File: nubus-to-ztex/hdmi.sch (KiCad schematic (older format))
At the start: 10 parts, among them J5 10029449-111RLF (HDMI A), U9 TPD12S016PWR

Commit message: some BoM optimization
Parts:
- C20: MPN CC0603KRX7R8BB103 -> 0603B103K500NT; URL https://www.lcsc.com/product-detail/Multilayer-Ceramic-Capacitors-MLCC-SMD-SMT_YAGEO-CC0603KRX7R8BB103_C327204.html -> https://www.lcsc.com/product-detail/Multilayer-Ceramic-Capacitors-MLCC-SMD-SMT_FH-Guangdong-Fenghua-Advanced-Tech-0603B103K500NT_C57112.html
- C22, C23, C24: MPN CC0603KRX7R8BB104 -> CC0603KRX7R9BB104; URL https://www.lcsc.com/product-detail/Multilayer-Ceramic-Capacitors-MLCC-SMD-SMT_YAGEO-CC0603KRX7R8BB104_C92490.html -> https://www.lcsc.com/product-detail/Multilayer-Ceramic-Capacitors-MLCC-SMD-SMT_YAGEO-CC0603KRX7R9BB104_C14663.html
- C7: MPN C0805V103KCRACTU -> C0805X103K501T; MPN-ALT (none) -> C0805V103KCRACTU; MPN-ALT2 (none) -> TCC0805X7R103K501FT; URL https://www.lcsc.com/product-detail/Multilayer-Ceramic-Capacitors-MLCC-SMD-SMT_KEMET-C0805V103KCRACTU_C2170011.html -> https://www.lcsc.com/product-detail/Multilayer-Ceramic-Capacitors-MLCC-SMD-SMT_IHHEC-HOLY-STONE-ENTERPRISE-CO-LTD-C0805X103K501T_C105950.html; URL-ALT (none) -> https://www.lcsc.com/product-detail/Multilayer-Ceramic-Capa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; URL-ALT2 (none) -> https://www.lcsc.com/product-detail/Multilayer-Ceramic-Capa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
- R9: value 1M 500V 2512 -> 1M 500V 1206; footprint Resistor_SMD:R_2512_6332Metric -> Resistor_SMD:R_1206_3216Metric; MPN AS25J1004ET -> HR1206J1M00P05Z; MPN-ALT (none) -> KTR18EZPF1004; URL https://www.lcsc.com/product-detail/Chip-Resistor-Surface-Mount_Ohmite-AS25J1004ET_C2546765.html -> https://www.lcsc.com/product-detail/Chip-Resistor-Surface-Mount_Ever-Ohms-Tech-HR1206J1M00P05Z_C175518.html; URL-ALT (none) -> https://www.lcsc.com/product-detail/Chip-Resistor-Surface-M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
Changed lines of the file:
@@
 F 3 "" H 7300 1700 50  0000 C CNN
 F 4 "www.yageo.com" H 7300 1700 50  0001 C CNN "MNF1_URL"
-F 5 "CC0603KRX7R8BB104" H 7300 1700 50  0001 C CNN "MPN"
+F 5 "CC0603KRX7R9BB104" H 7300 1700 50  0001 C CNN "MPN"
 F 6 "603-CC603KRX7R8BB104" H 7300 1700 50  0001 C CNN "Mouser"
 F 7 "?" H 7300 1700 50  0001 C CNN "Digikey"
@@
 F 9 "?" H 7300 1700 50  0001 C CNN "Koncar"
 F 10 "TB" H 7300 1700 50  0001 C CNN "Side"
-F 11 "https://www.lcsc.com/product-detail/Multilayer-Ceramic-Capacitors-MLCC-SMD-SMT_YAGEO-CC0603KRX7R8BB104_C92490.html" H 3000 6050 50  0001 C CNN "URL"
+F 11 "https://www.lcsc.com/product-detail/Multilayer-Ceramic-Capacitors-MLCC-SMD-SMT_YAGEO-CC0603KRX7R9BB104_C14663.html" H 3000 6050 50  0001 C CNN "URL"
 	1    7300 1700
 	1    0    0    -1
@@
 F 3 "" H 2250 1600 50  0000 C CNN
 F 4 "www.yageo.com" H 2250 1600 50  0001 C CNN "MNF1_URL"
-F 5 "CC0603KRX7R8BB104" H 2250 1600 50  0001 C CNN "MPN"
+F 5 "CC0603KRX7R9BB104" H 2250 1600 50  0001 C CNN "MPN"
 F 6 "603-CC603KRX7R8BB104" H 2250 1600 50  0001 C CNN "Mouser"
 F 7 "?" H 2250 1600 50  0001 C CNN "Digikey"
@@
 F 9 "?" H 2250 1600 50  0001 C CNN "Koncar"
 F 10 "TB" H 2250 1600 50  0001 C CNN "Side"
-F 11 "https://www.lcsc.com/product-detail/Multilayer-Ceramic-Capacitors-MLCC-SMD-SMT_YAGEO-CC0603KRX7R8BB104_C92490.html" H 2250 1600 50  0001 C CNN "URL"
+F 11 "https://www.lcsc.com/product-detail/Multilayer-Ceramic-Capacitors-MLCC-SMD-SMT_YAGEO-CC0603KRX7R9BB104_C14663.html" H 2250 1600 50  0001 C CNN "URL"
 	1    2250 1600
 	0    1    1    0
@@
 F 3 "" H 2450 1900 50  0000 C CNN
 F 4 "www.yageo.com" H 2450 1900 50  0001 C CNN "MNF1_URL"
-F 5 "CC0603KRX7R8BB104" H 2450 1900 50  0001 C CNN "MPN"
+F 5 "CC0603KRX7R9BB104" H 2450 1900 50  0001 C CNN "MPN"
 F 6 "603-CC603KRX7R8BB104" H 2450 1900 50  0001 C CNN "Mouser"
 F 7 "?" H 2450 1900 50  0001 C CNN "Digikey"
@@
 F 9 "?" H 2450 1900 50  0001 C CNN "Koncar"
 F 10 "TB" H 2450 1900 50  0001 C CNN "Side"
-F 11 "https://www.lcsc.com/product-detail/Multilayer-Ceramic-Capacitors-MLCC-SMD-SMT_YAGEO-CC0603KRX7R8BB104_C92490.html" H 3000 6050 50  0001 C CNN "URL"
+F 11 "https://www.lcsc.com/product-detail/Multilayer-Ceramic-Capacitors-MLCC-SMD-SMT_YAGEO-CC0603KRX7R9BB104_C14663.html" H 3000 6050 50  0001 C CNN "URL"
 	1    2450 1900
 	0    1    1    0
@@
 F 3 "" H 2250 1100 50  0000 C CNN
 F 4 "www.yageo.com" H 2250 1100 50  0001 C CNN "MNF1_URL"
-F 5 "CC0603KRX7R8BB103" H 2250 1100 50  0001 C CNN "MPN"
+F 5 "0603B103K500NT" H 2250 1100 50  0001 C CNN "MPN"
 F 6 "603-CC603KRX7R8BB103" H 2250 1100 50  0001 C CNN "Mouser"
-F 7 "https://www.lcsc.com/product-detail/Multilayer-Ceramic-Capacitors-MLCC-SMD-SMT_YAGEO-CC0603KRX7R8BB103_C327204.html" H 2250 1100 50  0001 C CNN "URL"
+F 7 "https://www.lcsc.com/product-detail/Multilayer-Ceramic-Capacitors-MLCC-SMD-SMT_FH-Guangdong-Fenghua-Advanced-Tech-0603B103K500NT_C57112.html" H 2250 1100 50  0001 C CNN "URL"
 	1    2250 1100
 	0    1    1    0
@@
 F 2 "Capacitor_SMD:C_0805_2012Metric" H 8238 4500 50  0001 C CNN
 F 3 "~" H 8200 4650 50  0001 C CNN
-F 4 "C0805V103KCRACTU" H 8200 4650 50  0001 C CNN "MPN"
-F 5 "https://www.lcsc.com/product-detail/Multilayer-Ceramic-Capacitors-MLCC-SMD-SMT_KEMET-C0805V103KCRACTU_C2170011.html" H 8200 4650 50  0001 C CNN "URL"
+F 4 "C0805V103KCRACTU" H 8200 4650 50  0001 C CNN "MPN-ALT"
+F 5 "https://www.lcsc.com/product-detail/Multilayer-Ceramic-Capacitors-MLCC-SMD-SMT_KEMET-C0805V103KCRACTU_C2170011.html" H 8200 4650 50  0001 C CNN "URL-ALT"
+F 6 "TCC0805X7R103K501FT" H 8200 4650 50  0001 C CNN "MPN-ALT2"
+F 7 "https://www.lcsc.com/product-detail/Multilayer-Ceramic-Capacitors-MLCC-SMD-SMT_CCTC-TCC0805X7R103K501FT_C282729.html" H 8200 4650 50  0001 C CNN "URL-ALT2"
+F 8 "C0805X103K501T" H 8200 4650 50  0001 C CNN "MPN"
+F 9 "https://www.lcsc.com/product-detail/Multilayer-Ceramic-Capacitors-MLCC-SMD-SMT_IHHEC-HOLY-STONE-ENTERPRISE-CO-LTD-C0805X103K501T_C105950.html" H 8200 4650 50  0001 C CNN "URL"
 	1    8200 4650
 	1    0    0    -1
@@
 AR Path="/61B62C00/641A2763" Ref="R9"  Part="1"
 F 0 "R9" H 8570 4696 50  0000 L CNN
-F 1 "1M 500V 2512" H 8570 4605 50  0000 L CNN
-F 2 "Resistor_SMD:R_2512_6332Metric" V 8430 4650 50  0001 C CNN
+F 1 "1M 500V 1206" H 8570 4605 50  0000 L CNN
+F 2 "Resistor_SMD:R_1206_3216Metric" V 8430 4650 50  0001 C CNN
 F 3 "~" H 8500 4650 50  0001 C CNN
-F 4 "AS25J1004ET" H 8500 4650 50  0001 C CNN "MPN"
-F 5 "https://www.lcsc.com/product-detail/Chip-Resistor-Surface-Mount_Ohmite-AS25J1004ET_C2546765.html" H 8500 4650 50  0001 C CNN "URL"
+F 4 "HR1206J1M00P05Z" H 8500 4650 50  0001 C CNN "MPN"
+F 5 "https://www.lcsc.com/product-detail/Chip-Resistor-Surface-Mount_Ever-Ohms-Tech-HR1206J1M00P05Z_C175518.html" H 8500 4650 50  0001 C CNN "URL"
+F 6 "KTR18EZPF1004" H 8500 4650 50  0001 C CNN "MPN-ALT"
+F 7 "https://www.lcsc.com/product-detail/Chip-Resistor-Surface-Mount_ROHM-Semicon-KTR18EZPF1004_C253347.html" H 8500 4650 50  0001 C CNN "URL-ALT"
 	1    8500 4650
 	1    0    0    -1

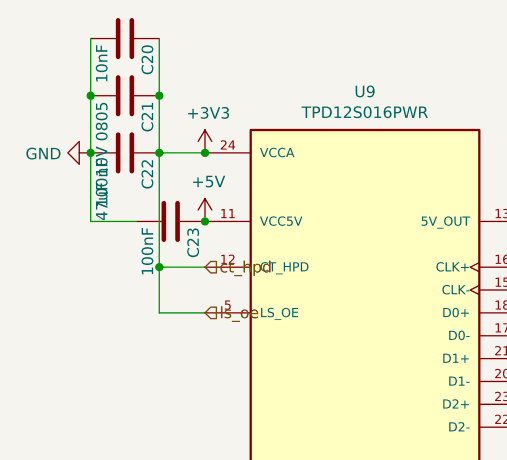
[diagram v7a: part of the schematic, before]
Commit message: even more JLCPCB BoM optimization
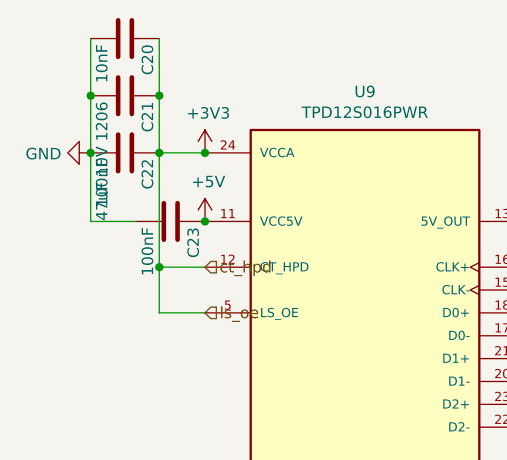
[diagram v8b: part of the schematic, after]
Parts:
- C21: value 47uF 10V 0805 -> 47uF 10V 1206; footprint Capacitor_SMD:C_0805_2012Metric -> Capacitor_SMD:C_1206_3216Metric; MPN C2012X5R1A476MTJ00E -> CL31A476MPHNNNE; URL https://www.lcsc.com/product-detail/Multilayer-Ceramic-Capacitors-MLCC-SMD-SMT_TDK-C2012X5R1A476MTJ00E_C76636.html -> https://www.lcsc.com/product-detail/Multilayer-Ceramic-Capacitors-MLCC-SMD-SMT_Samsung-Electro-Mechanics-CL31A476MPHNNNE_C96123.html
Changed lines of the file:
@@
 AR Path="/61B62C00/6148D34D" Ref="C21"  Part="1"
 F 0 "C21" H 2275 1450 50  0000 L CNN
-F 1 "47uF 10V 0805" H 2275 1250 50  0000 L CNN
-F 2 "Capacitor_SMD:C_0805_2012Metric" H 2288 1200 50  0001 C CNN
+F 1 "47uF 10V 1206" H 2275 1250 50  0000 L CNN
+F 2 "Capacitor_SMD:C_1206_3216Metric" H 2288 1200 50  0001 C CNN
 F 3 "" H 2250 1350 50  0000 C CNN
 F 4 "GRM21BR61A476ME15L # 10V" H 2250 1350 50  0001 C CNN "MPN-ALT3"
@@
 F 9 "https://www2.mouser.com/ProductDetail/?qs=u16ybLDytRYYQtTToF3RWA%3D%3D" H 2250 1350 50  0001 C CNN "URL-PREV"
 F 10 "https://lcsc.com/product-detail/Multilayer-Ceramic-Capacitors-MLCC-SMD-SMT_TDK-C2012X5R1A476MTJ00E_C76636.html" H 2250 1350 50  0001 C CNN "URL-ALT"
-F 11 "C2012X5R1A476MTJ00E" H 2250 1350 50  0001 C CNN "MPN"
-F 12 "https://www.lcsc.com/product-detail/Multilayer-Ceramic-Capacitors-MLCC-SMD-SMT_TDK-C2012X5R1A476MTJ00E_C76636.html" H 2250 1350 50  0001 C CNN "URL"
+F 11 "CL31A476MPHNNNE" H 2250 1350 50  0001 C CNN "MPN"
+F 12 "https://www.lcsc.com/product-detail/Multilayer-Ceramic-Capacitors-MLCC-SMD-SMT_Samsung-Electro-Mechanics-CL31A476MPHNNNE_C96123.html" H 2250 1350 50  0001 C CNN "URL"
 	1    2250 1350
 	0    1    1    0
